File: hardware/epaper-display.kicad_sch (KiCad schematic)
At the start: 57 parts, among them J1 AES200200A00 FPC, J2 USB-C, J3 LiPo JST-PH, J4 I2C temp (optional), J5 UART, J6 GPIO expansion, Q1 Si1304BDL / NX3008NBK, SW1 EN/RESET, SW2 BOOT, SW3 BTN_UP, SW4 BTN_DOWN, SW5 BTN_LEFT, SW6 BTN_RIGHT, SW7 BTN_SELECT, SW8 BTN_CANCEL, U1 ESP32-S3-WROOM-1-N8, U2 MCP73831T-2ACI/OT, U3 MCP1825S-3302E/DB

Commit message: hardware: fix schematic issues found in datasheet review
Reviewed the netlist against all six component datasheets. Fixes below;
each one names the datasheet clause it comes from.

Correctness:

- R6 (charge LED) now returns to VBUS instead of +3V3. MCP73831 Fig 6-1
  puts RLED on VDD. Returning it to the regulated rail forward-biased the
  LED from the battery into the high-Z STAT pin whenever USB was absent,
  back-feeding the charger VDD node and the USB-C VBUS contact off the
  cell and breaking the "all I/O <= VDD + 0.3 V" absolute maximum.
- R15 (GPIO3 strap) populated, was DNP. WROOM-1 datasheet 4.4: GPIO3 has
  no internal pull resistor and "must be controlled by the external
  circuit that cannot be in a high impedance state".
- J2 rewritten against the real 16-pad USB-C pinout (A1..A12/B1..B12/S1),
  verified against the KiCad 8.0.9 USB_C_Receptacle_GCT_USB4085 footprint
  rather than assumed. Both rows are paralleled so the cable works either
  way up; CC1/CC2 keep separate 5.1k Rd.
- R3/R4 22R -> 0R on USB D+/D-. The S3 USB PHY has integrated series
  termination; 22R per leg added 44R differential to a 90R pair.
- Battery protection: J3 now requires a cell with an integrated
  protection PCM (no over-discharge protection exists on-board), and D6
  crowbars a reverse-polarity cell instead of letting it drive VBAT
  negative through U2/U3 ESD structures. The two are one mechanism.
- D7 (SMAJ5.0A) clamps VBUS transients, per MCP73831 6.1.1.2.
- D1 (USBLC6-2SC6) populated; SOT-23-6 is hand-solderable.

Power:

- R5 4.7k -> 10k (213 mA -> 100 mA charge). At 213 mA the SOT-23-5 saw
  0.57 W worst case, 132 C rise at the datasheet's 230 C/W minimum-copper
  theta-JA, which drove it into thermal regulation.
- R9/R10 100k -> 1M. The divider sits across the cell permanently and
  drew 21 uA, roughly triple the S3's own deep-sleep current.
- R14/R16 10k -> 100k, saving 330 uA whenever driven against.
- Rail buffering: C18 4.7uF on +3V3 and C20 100uF on VBAT. Most 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
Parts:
- removed J2: USB-C, Connector_USB:USB_C_Receptacle_GCT_USB4085, symbol epaper:USB_C_Receptacle
- added C18: 4.7uF, Capacitor_SMD:C_1206_3216Metric, symbol epaper:C
- added C20: 100uF, Capacitor_SMD:C_1206_3216Metric, symbol epaper:C
- added D6: SS14 (reverse-polarity clamp), Diode_SMD:D_SMA, symbol epaper:D_Schottky
- added D7: SMAJ5.0A, Diode_SMD:D_SMA, symbol epaper:D_TVS
- added J2: USB-C 2.0 receptacle, Connector_USB:USB_C_Receptacle_GCT_USB4085, symbol epaper:USB_C_Receptacle_USB2.0
- added R17, R18, R19, R20, R21, R22: 100k, Resistor_SMD:R_0805_2012Metric, symbol epaper:R
- added R23: 0, Resistor_SMD:R_0805_2012Metric, symbol epaper:R
- C10, C11, C14, C15, C16, C17, C9: value 1uF/25V -> 1uF/50V
- D1: value USBLC6-2SC6 (optional) -> USBLC6-2SC6; now fitted
- J3: value LiPo JST-PH -> LiPo JST-PH (PROTECTED cell)
- L1: footprint Inductor_SMD:L_1210_3225Metric -> Inductor_SMD:L_Sunlord_MWSA0402S
- R10, R9: value 100k -> 1M
- R14, R16: value 10k -> 100k
- R15: value 10k (DNP) -> 10k; now fitted
- R3, R4: value 22 -> 0
- R5: value 4.7k -> 10k
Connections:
- net +3V3: now also C18.1, R17.1, R18.1, R19.1, R20.1, R21.1, R22.1, R23.2; no longer J1.19 (VPP), R6.1
- net CC1: now also J2.A5 (CC1)
- net CC2: now also J2.B5 (CC2)
- net GND: now also C18.2, C20.2, D6.1 (A), D7.1 (A), J2.A1 (GND), J2.A12 (GND), J2.B1 (GND), J2.B12 (GND), J2.S1 (SHIELD)
- net USB_DM: now also J2.A7 (D-), J2.B7 (D-)
- net USB_DP: now also J2.A6 (D+), J2.B6 (D+)
- net VBAT: now also C20.1, D6.2 (K)
- net VBUS: now also R6.1, D7.2 (K), J2.A4 (VBUS), J2.A9 (VBUS), J2.B4 (VBUS), J2.B9 (VBUS)
- net EXP_IO10 renamed BTN_DOWN
- net BTN_DOWN: now also R18.2
- net EXP_IO11 renamed BTN_LEFT
- net BTN_LEFT: now also R19.2
- net EXP_IO12 renamed BTN_RIGHT
- net BTN_RIGHT: now also R20.2
- net EXP_IO13 renamed BTN_SELECT
- net BTN_SELECT: now also R21.2
- net EXP_IO14 renamed BTN_CANCEL
- net BTN_CANCEL: now also R22.2
- net EXP_IO2 renamed BTN_UP
- net BTN_UP: now also R17.2
- new net EPD_VPP: J1.19 (VPP), R23.1
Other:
- note added: "Buttons SW3-SW8 use external 100k pull-ups (R17-R22) so they hold a defined level"
- note added: "J3 REQUIRES a LiPo cell with an integrated protection PCM. Nothing on this board"
- note added: "U3 Iq is 120uA typ / 220uA max and dominates the standby budget - swap for a"
- note added: "Verify cell polarity before first plug-in: JST-PH wiring varies between vendors."
- note added: "stops over-discharge, and D6 relies on that PCM to clear a reverse-polarity fault."
- note added: "sub-30uA LDO (TLV75733P / AP2112K) if standby current matters."
- note added: "through deep sleep; firmware may still enable RTC pull-ups harmlessly in parallel."

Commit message: hardware: swap MCP1825S for TLV75733P (1A, 25uA Iq)
The MCP1825S's 120 uA typ / 220 uA max quiescent current was ~15x the
ESP32-S3's own deep-sleep draw and made the regulator the entire standby
budget on a board that is asleep 99.98% of the time.

Linear, not a switcher. Four reasons, in README 2:

- At a 0.023% duty cycle the efficiency gap is worth ~0.1 mWh/day out of
  a ~5 mWh/day budget -- less than the regulator's own Iq contributes.
- A plain buck cannot even do the job: a single LiPo spans 4.2-3.0 V,
  which straddles the 3.3 V output. Covering the full cell range needs a
  buck-boost, and those run 25-50 uA Iq, so there is no Iq win.
- The genuinely low-Iq switchers (TPS62840, 60 nA) ship only in SOT-583
  and WSON, which breaks the no-reflow constraint the BOM is built on.
- A switching node would sit next to the panel's own boost converter and
  a 500 kOhm-source-impedance ADC sense divider.

Since standby dominates, Iq is the only figure of merit that moves the
needle, and that is something a linear part supplies fine. 25 uA is also
the knee: getting to 1 uA means dropping to a 200 mA part (TPS7A05),
which cannot serve a 355 mA TX burst, and the cell's own self-discharge
starts to dominate anyway.

Verified against SBVS322C (added to components/):

- Iq 25 uA typ / 31 uA max at 25 C, 33 uA max to +85 C (5.5)
- VIN 1.45-5.5 V, current limit 1.2 A min (5.5)
- Dropout 425 mV max at 1 A, and 7.1.2 states VDO scales linearly with
  current, so ~212 mV at 500 mA vs the MCP1825S's 350 mV. VBAT_min for
  regulation drops 3.65 V -> 3.51 V, recovering some of the discharge
  curve the previous revision gave away.
- COUT 0.47 uF to 200 uF (7.1.1). The MCP1825S's 22 uF ceiling was what
  forced bulk onto VBAT last revision; that constraint is gone, so C18
  goes 4.7 -> 47 uF on +3V3 where the load transient actually is.

Two things got worse and are documented rather than glossed:

- RthJA 231 C/W for the DBV package vs a SOT-223 tab. Worst case is
  0.45 W (full c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
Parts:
- removed U3: MCP1825S-3302E/DB, Package_TO_SOT_SMD:SOT-223-3_TabPin2, symbol epaper:MCP1825S-3302
- added U3: TLV75733PDBVR, Package_TO_SOT_SMD:SOT-23-5, symbol epaper:LDO_SOT23_5
- C18: value 4.7uF -> 47uF
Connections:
- net +3V3: now also U3.5 (OUT)
- net GND: now also U3.2 (GND)
- net VBAT: now also U3.1 (IN), U3.3 (EN)
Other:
- note added: "U3 (SOT-23-5, 1=IN 2=GND 3=EN 4=NC 5=OUT) accepts TLV75733PDBVR / AP2112K-3.3 /"
- note added: "U3 is the DBV package: RthJA 231 C/W, no thermal pad. Fine for this board's"
- note added: "XC6220B331MR unchanged. EN is tied to IN - do not leave it floating."
- note added: "burst load, but do NOT draw a sustained 500mA from +3V3 via J6."
- note removed: "U3 Iq is 120uA typ / 220uA max and dominates the standby budget - swap for a"
- note removed: "sub-30uA LDO (TLV75733P / AP2112K) if standby current matters."

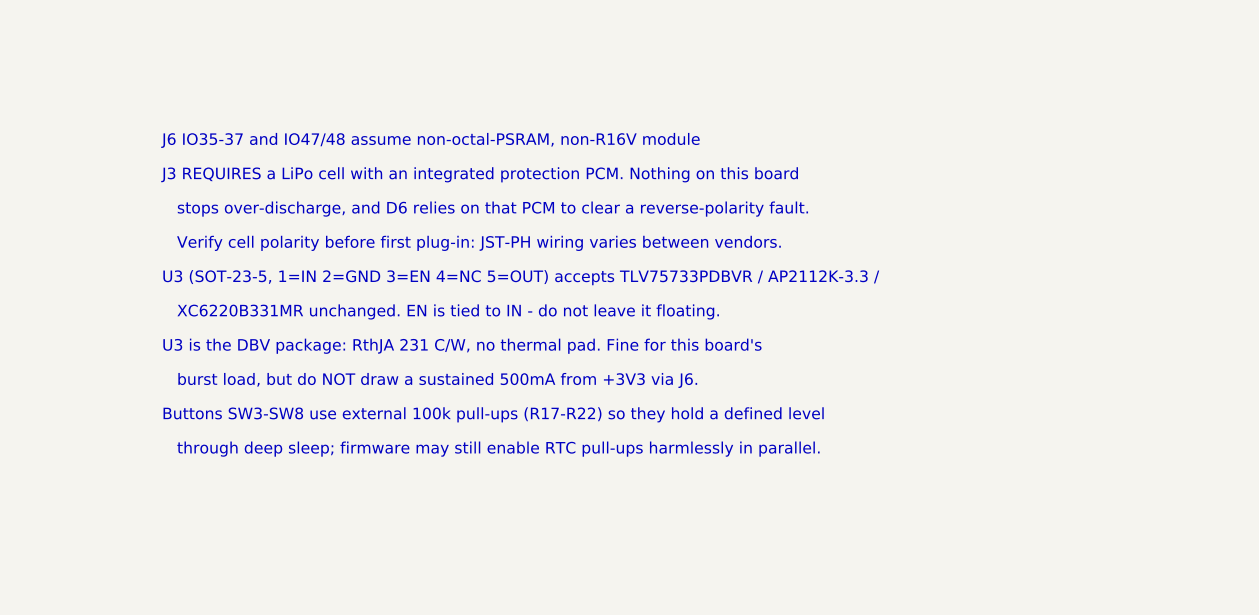
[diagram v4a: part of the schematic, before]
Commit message: hardware: target the Turnigy BoltX LiHV pack + inline 1S protection
The chosen cell is a Turnigy BoltX LiHV 1S 300mAh 3.8V 80C whoop pack.
No schematic change follows from it, but three things needed saying and
one of them is a safety matter.

The pack is an unprotected drone cell. Whoop packs ship as bare cells --
maximum discharge rate, minimum weight, low-voltage cutoff delegated to
the flight controller. That is incompatible with this board in two ways:
nothing here stops over-discharge, and D6 shorts a reversed cell *on
purpose*, relying on the pack's protection to clear the fault. An 80C
300mAh cell is rated for 24 A; an SS14 across that with nothing to
interrupt it is worse than having no crowbar at all. An inline
DW01A-class 1S protection PCB between cell and connector is therefore
mandatory, not advisory. With it fitted the DW01A trips in microseconds
and the SS14's 50 A / 8.3 ms IFSM rides through comfortably.

U2 stays the -2 (4.20 V) option and must not become the -3 (4.35 V) one,
even though the cell is LiHV and the 4.35 V variant exists
(MCP73831T-3ACI/OT, datasheet 1.0 VREG). Standard DW01A boards cut off
overcharge near 4.30 V, so a 4.35 V charger would fight the protection
circuit. Charging an HV cell to 4.20 V is an undercharge -- entirely
safe, costs ~13% of nameplate capacity, and improves calendar life on a
device that sits near full charge for months.

The 80C rating is 60x more than the 1.2C we draw, but it buys very low
internal resistance, which retires the sag concern raised for a generic
300mAh cell:

  generic 300mAh, 300mOhm   TX 355mA  sag 106mV -> cell OCV >= 3.56 V
  80C cell + PCM, ~80mOhm   TX 355mA  sag  28mV -> cell OCV >= 3.48 V
  80C cell + PCM, ~80mOhm   500mA     sag  40mV -> cell OCV >= 3.55 V

Serialising Wi-Fi and panel refresh is still the right firmware shape
but is no longer load-bearing for the power budget.

Budget: ~930 mWh usable after the 4.20 V derate and a 3.4 V firmware
cutoff; standby rises to ~46 uA once the DW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
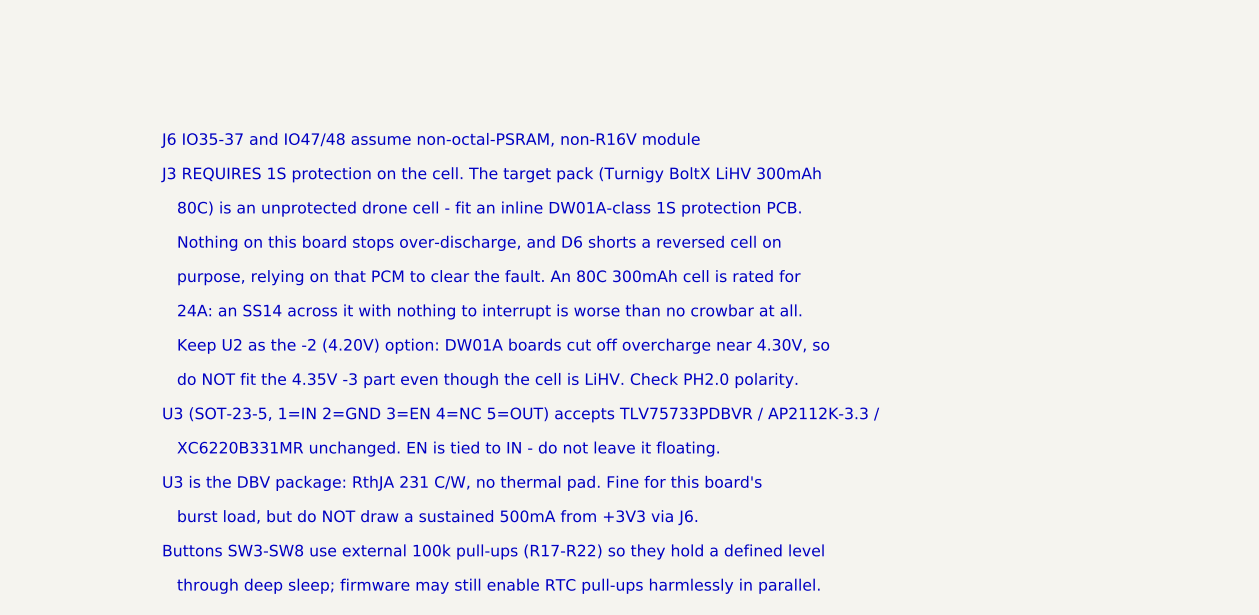
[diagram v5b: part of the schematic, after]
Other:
- note added: "24A: an SS14 across it with nothing to interrupt is worse than no crowbar at all."
- note added: "80C) is an unprotected drone cell - fit an inline DW01A-class 1S protection PCB."
- note added: "J3 REQUIRES 1S protection on the cell. The target pack (Turnigy BoltX LiHV 300mAh"
- note added: "Keep U2 as the -2 (4.20V) option: DW01A boards cut off overcharge near 4.30V, so"
- note added: "Nothing on this board stops over-discharge, and D6 shorts a reversed cell on"
- note added: "do NOT fit the 4.35V -3 part even though the cell is LiHV. Check PH2.0 polarity."
- note added: "purpose, relying on that PCM to clear the fault. An 80C 300mAh cell is rated for"
- note removed: "J3 REQUIRES a LiPo cell with an integrated protection PCM. Nothing on this board"
- note removed: "Verify cell polarity before first plug-in: JST-PH wiring varies between vendors."
- note removed: "stops over-discharge, and D6 relies on that PCM to clear a reverse-polarity fault."

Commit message: hardware: add on-board 1S protection (DW01A + FS8205A); remove D6
Moves the 1S protection from an inline module onto the board, so J3 is
now the raw cell rather than a protected pack. Wired exactly as the
DW01A datasheet application circuit (p.9) draws it:

  J3.1 = B+ = VBAT (high side never switched)
  J3.2 = B- on its own net (BATT_NEG), NOT board GND
  R24 100R  VBAT -> U4 VDD ; C21 100nF VDD-VSS ; U4 VSS -> B-
  Q2 half 1 = discharge control (G1 <- DO, S1 = B-)
  Q2 half 2 = charge control    (G2 <- CO, S2 = GND/P-)
  Q2 D1/D2 commoned ; U4 VM -> R25 1k -> GND

The gate/source pairing is set by the DW01A, which turns the discharge
FET off by driving DO to VSS and the charge FET off by driving CO to VM
(datasheet p.6), so each gate must reference its own source.

Protection now present: overcharge 4.30V +/-50mV (110ms), over-discharge
2.50V +/-75mV (55ms), over-current 0.15V across the FETs (7ms), short
circuit (200-600us). Q2 adds 2 x 20.5 mOhm to the ground return, ~20 mV
at a 500 mA burst.

D6 (SS14 reverse-polarity crowbar) is REMOVED, deliberately. Its whole
rationale was "short a reversed cell and let the pack's PCM interrupt
it". With protection on-board, a reversed connector is applied upstream
of U4/Q2, so nothing is left to clear the fault -- and an 80C 300mAh
cell sources ~24 A into a 1 A diode. That made the board's designated
short-circuit path a fire risk rather than a safeguard.

The residual risk is stated rather than glossed: the board now has NO
reverse-polarity protection. A reversed cell reverse-biases U4 (VDD
3.8 V below VSS against a -0.3 V abs max, current-limited to ~31 mA by
R24) and will probably destroy it. Mitigation is the keyed connector
plus the documented meter check.

Also documents a corner: MCP73831-2 VREG max is 4.232 V and DW01A VOC
min is 4.250 V at 25C (18 mV margin) but 4.220 V over -40..85C, so the
bands can overlap by 12 mV. Symptom would be a latched overcharge trip
that needs USB unplugged to clear (DW01A p.6), not dam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
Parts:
- removed D6: SS14 (reverse-polarity clamp), Diode_SMD:D_SMA, symbol epaper:D_Schottky
- added C21: 100nF, Capacitor_SMD:C_0805_2012Metric, symbol epaper:C
- added Q2: FS8205A, Package_TO_SOT_SMD:SOT-23-6, symbol epaper:FS8205A
- added R24: 100, Resistor_SMD:R_0805_2012Metric, symbol epaper:R
- added R25: 1k, Resistor_SMD:R_0805_2012Metric, symbol epaper:R
- added U4: DW01A, Package_TO_SOT_SMD:SOT-23-6, symbol epaper:DW01A
- J3: value LiPo JST-PH (PROTECTED cell) -> LiPo cell (B+/B-)
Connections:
- net GND: now also Q2.3 (S2), R25.2; no longer J3.2
- net VBAT: now also R24.1
- new net BATT_NEG: C21.2, J3.2, Q2.1 (S1), U4.6 (VSS)
- new net PROT_CO: Q2.4 (G2), U4.3 (CO)
- new net PROT_DO: Q2.2 (G1), U4.1 (DO)
- new net PROT_MID: Q2.5 (D2), Q2.6 (D1)
- new net PROT_VDD: C21.1, R24.2, U4.5 (VDD)
- new net PROT_VM: R25.1, U4.2 (VM)
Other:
- note added: "1S protection (U4 DW01A + Q2 FS8205A) is on-board, in the low side between B-"
- note added: "A METER before first plug-in - a reversed cell will destroy U4."
- note added: "J3 is the RAW CELL, not a protected pack: pin 1 = B+, pin 2 = B- on its own net."
- note added: "Keep U2 as the -2 (4.20V) option: U4 trips overcharge at 4.30V, so the 4.35V -3"
- note added: "Q2 pin numbering is the industry-standard 8205A mapping - the FS8205A datasheet"
- note added: "There is NO reverse-polarity protection. The old D6 crowbar was removed: it would"
- note added: "and GND, per the DW01A datasheet application circuit p.9."
- note added: "and an 80C 300mAh cell sources ~24A into a 1A diode. CHECK PH2.0 POLARITY WITH"
- note added: "now sit downstream of a reversed connector with nothing left to clear the fault,"
- note added: "part would fight the protection. Do NOT fit it even though the cell is LiHV."
- note added: "states no pin numbers and KiCad has no symbol. BUZZ IT OUT on the first board."
- note removed: "24A: an SS14 across it with nothing to interrupt is worse than no crowbar at all."
- note removed: "80C) is an unprotected drone cell - fit an inline DW01A-class 1S protection PCB."
- note removed: "J3 REQUIRES 1S protection on the cell. The target pack (Turnigy BoltX LiHV 300mAh"
- note removed: "Keep U2 as the -2 (4.20V) option: DW01A boards cut off overcharge near 4.30V, so"
- note removed: "Nothing on this board stops over-discharge, and D6 shorts a reversed cell on"
- note removed: "do NOT fit the 4.35V -3 part even though the cell is LiHV. Check PH2.0 polarity."
- note removed: "purpose, relying on that PCM to clear the fault. An 80C 300mAh cell is rated for"
